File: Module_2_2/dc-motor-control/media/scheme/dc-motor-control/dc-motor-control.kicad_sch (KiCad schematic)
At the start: 9 parts, among them M1 5V DC Motor, Q1 2222A, U1 ESP32-S3-WROOM-1

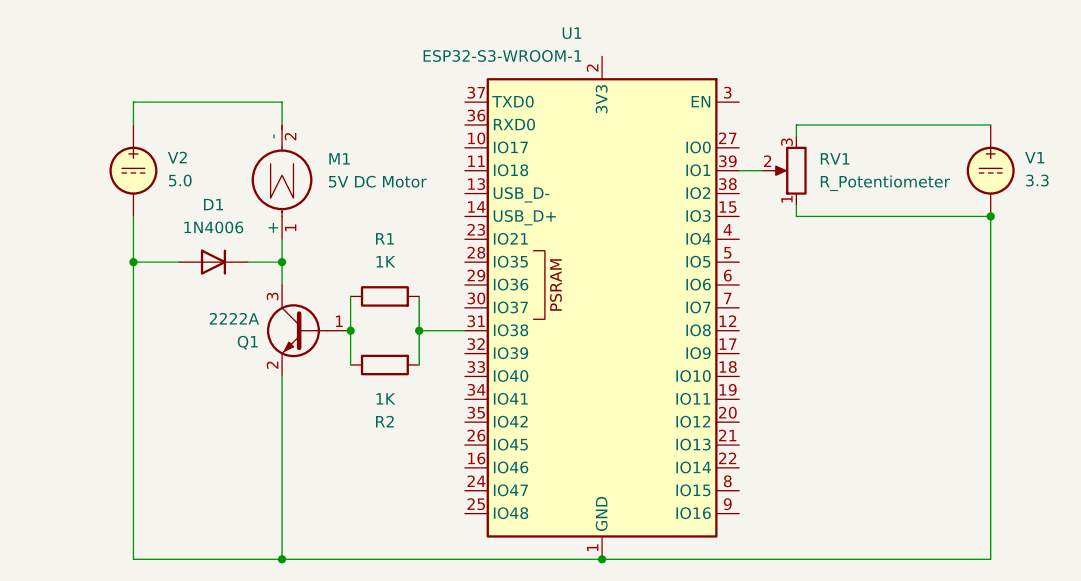
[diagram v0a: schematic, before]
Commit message: Додано конфігурацію і контроль PWM
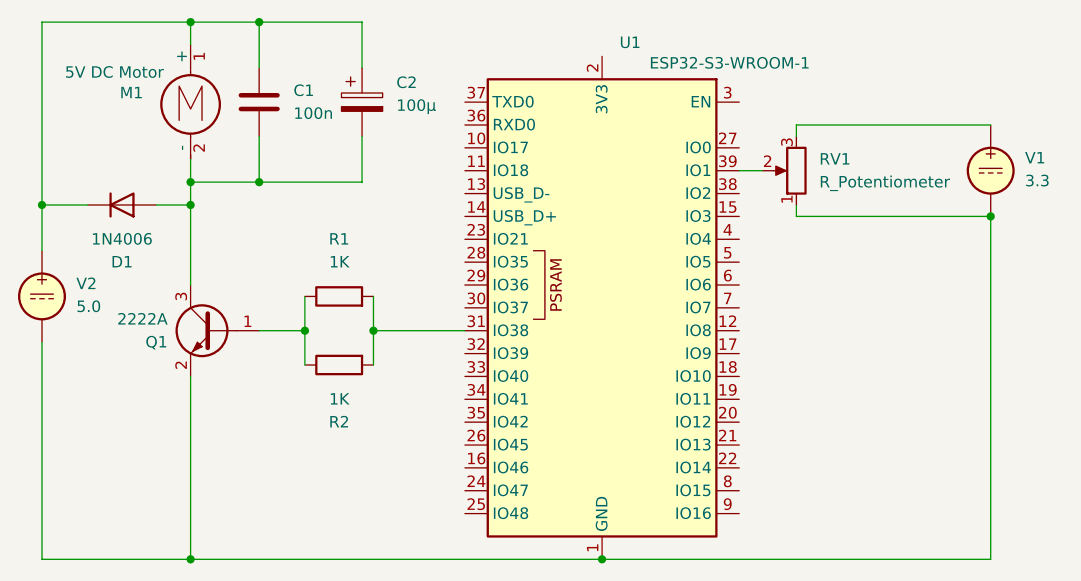
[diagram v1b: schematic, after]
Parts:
- added C1: 100n, symbol Device:C
- added C2: 100μ, symbol Device:C_Polarized
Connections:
- net at D1.1 (K), M1.1 (+): now also V2.1, C1.1, C2.1; no longer Q1.3 (C)
- net at M1.2 (-): now also D1.2 (A), Q1.3 (C), C1.2, C2.2; no longer V2.1
- net at Q1.2 (E), RV1.1, U1.1 (GND)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: no longer D1.2 (A)
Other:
- moved on the sheet: D1, M1, Q1, R1, R2, V2
